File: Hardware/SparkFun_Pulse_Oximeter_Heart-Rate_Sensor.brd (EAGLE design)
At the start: 5 parts, among them U1 MAX30101EFD+T, U2 MAX32664GWEA+T, U3 1.8V/100mA

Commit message: Adds a few parts (end of day merge)
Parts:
- added U$2: PAM2401, SparkFun-IC-Power:MSOP8
- moved U3 10.5 mm to (7.87, 17.8), turned to 0 degrees
- moved U2 7.89 mm to (12.7, 18.0)
- moved U1 3.54 mm to (12.7, 12.7)
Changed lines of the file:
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@@
 </element>
 <element name="U$1" library="SparkX" package="QWIIC_BOARD_MOUNT_NOHOLES" value="QWIIC_BOARD_OUTLINENH" x="12.7" y="12.7" smashed="yes"/>
-<element name="U1" library="temp" package="14_PIN_OESIP" value="MAX30101EFD+T" x="11.43" y="16.002" smashed="yes">
-<attribute name="NAME" x="10.43" y="22.002" size="1" layer="25"/>
-<attribute name="PROD_ID" value="IC-14270" x="11.43" y="16.002" size="1.778" layer="27" font="vector" ratio="15" display="off"/>
-<attribute name="VALUE" x="10.43" y="14.605" size="1" layer="27"/>
+<element name="U3" library="SparkFun-IC-Power" package="SC70" value="1.8V/100mA" x="7.874" y="17.78" smashed="yes">
+<attribute name="NAME" x="6.604" y="17.78" size="0.6096" layer="25" font="vector" ratio="20" rot="R90" align="bottom-center"/>
+<attribute name="PROD_ID" value="VREG-08428" x="7.874" y="17.78" size="1.778" layer="27" font="vector" ratio="15" display="off"/>
+<attribute name="VALUE" x="9.144" y="17.78" size="0.6096" layer="27" font="vector" ratio="20" rot="R90" align="top-center"/>
 </element>
-<element name="U2" library="temp" package="16_PIN_WLP" value="MAX32664GWEA+T" x="10.668" y="10.414" smashed="yes">
-<attribute name="NAME" x="10.668" y="12.414" size="1" layer="25"/>
-<attribute name="PROD_ID" value="IC-14271" x="10.668" y="10.414" size="1.778" layer="27" font="vector" ratio="15" display="off"/>
-<attribute name="VALUE" x="10.668" y="8.914" size="1" layer="27"/>
+<element name="U$2" library="SparkFun-IC-Power" package="MSOP8" value="PAM2401" x="12.446" y="6.604" smashed="yes" rot="R90">
+<attribute name="NAME" x="13.716" y="4.064" size="0.4064" layer="25" rot="R180"/>
+<attribute name="PROD_ID" value="IC-13769" x="12.446" y="6.604" size="1.778" layer="27" rot="R90" display="off"/>
+<attribute name="VALUE" x="13.716" y="9.144" size="0.4064" layer="27" rot="R180"/>
 </element>
-<element name="U3" library="SparkFun-IC-Power" package="SC70" value="1.8V/100mA" x="18.034" y="20.32" smashed="yes" rot="R90">
-<attribute name="NAME" x="18.034" y="19.05" size="0.6096" layer="25" font="vector" ratio="20" rot="R180" align="bottom-center"/>
-<attribute name="PROD_ID" value="VREG-08428" x="18.034" y="20.32" size="1.778" layer="27" font="vector" ratio="15" rot="R90" display="off"/>
-<attribute name="VALUE" x="18.034" y="21.59" size="0.6096" layer="27" font="vector" ratio="20" rot="R180" align="top-center"/>
+<element name="U1" library="temp" package="14_PIN_OESIP" value="MAX30101EFD+T" x="12.7" y="12.7" smashed="yes">
+<attribute name="NAME" x="10.062459375" y="15.909809375" size="1" layer="25"/>
+<attribute name="PROD_ID" value="IC-14270" x="12.7" y="12.7" size="1.778" layer="27" display="off"/>
+<attribute name="VALUE" x="10.062459375" y="8.512809375" size="1" layer="27"/>
+</element>
+<element name="U2" library="temp" package="16_PIN_WLP" value="MAX32664GWEA+T" x="12.7" y="18.034" smashed="yes">
+<attribute name="NAME" x="11.908" y="19.252" size="1" layer="25"/>
+<attribute name="PROD_ID" value="IC-14271" x="12.7" y="18.034" size="1.778" layer="27" display="off"/>
+<attribute name="VALUE" x="11.908" y="15.752" size="1" layer="27"/>
 </element>
 </elements>
@@
 <contactref element="U1" pad="P11"/>
 <contactref element="U2" pad="P$3"/>
-<wire x1="14.275" y1="18.801" x2="11.628" y2="11.714" width="0" layer="19" extent="1-1"/>
+<wire x1="13.907459375" y1="12.708809375" x2="12.868" y2="18.552" width="0" layer="19" extent="1-1"/>
 </signal>
 <signal name="GND">
@@
 <contactref element="U1" pad="P12"/>
 <contactref element="U2" pad="P$13"/>
-<wire x1="11.875" y1="18.801" x2="11.278" y2="11.364" width="0" layer="19" extent="1-1"/>
-<wire x1="14.275" y1="19.601" x2="11.875" y2="18.801" width="0" layer="19" extent="1-1"/>
+<wire x1="11.507459375" y1="12.708809375" x2="12.518" y2="18.202" width="0" layer="19" extent="1-1"/>
+<wire x1="13.907459375" y1="13.508809375" x2="11.507459375" y2="12.708809375" width="0" layer="19" extent="1-1"/>
 </signal>
 <signal name="VDD_LED">
 <contactref element="U1" pad="P10"/>
 <contactref element="U1" pad="P9"/>
-<wire x1="14.275" y1="17.201" x2="14.275" y2="18.001" width="0" layer="19" extent="1-1"/>
+<wire x1="13.907459375" y1="11.108809375" x2="13.907459375" y2="11.908809375" width="0" layer="19" extent="1-1"/>
 </signal>
 <signal name="VCORE">

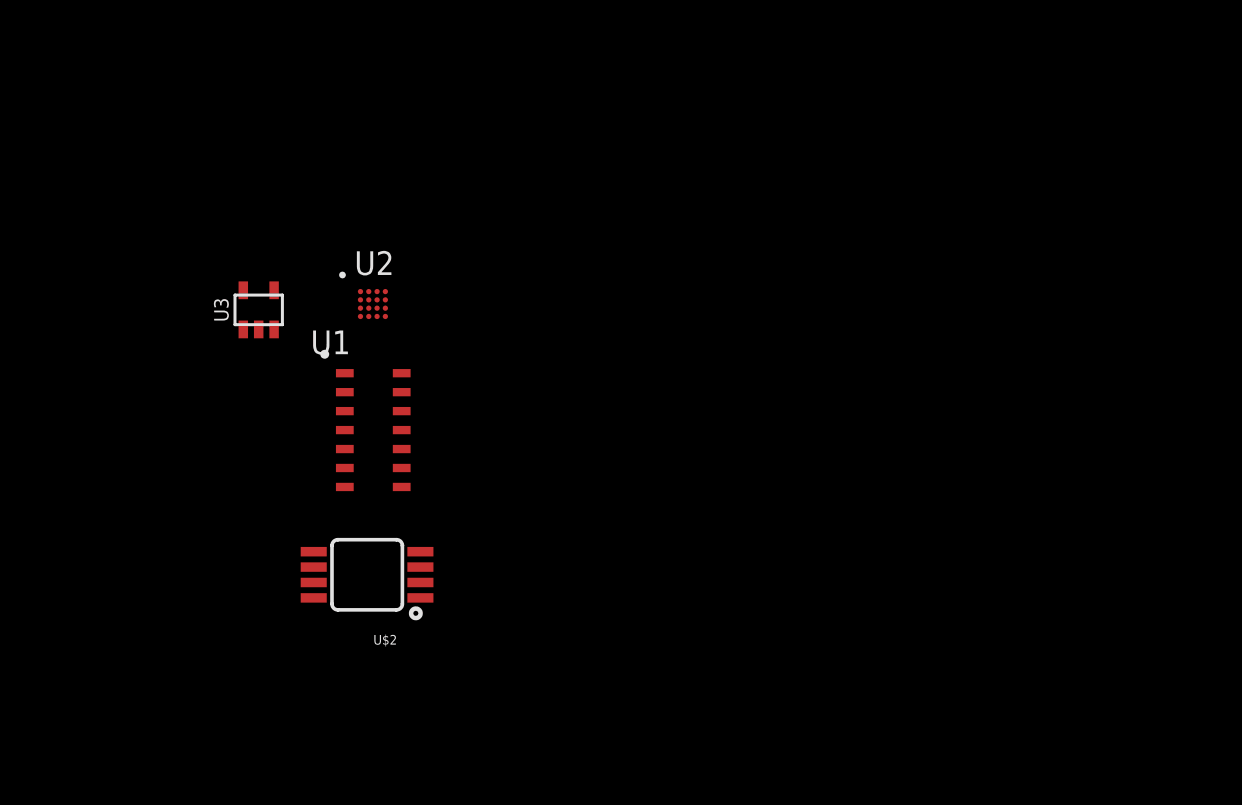
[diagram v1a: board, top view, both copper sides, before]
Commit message: Adds parts to DC-DC converter
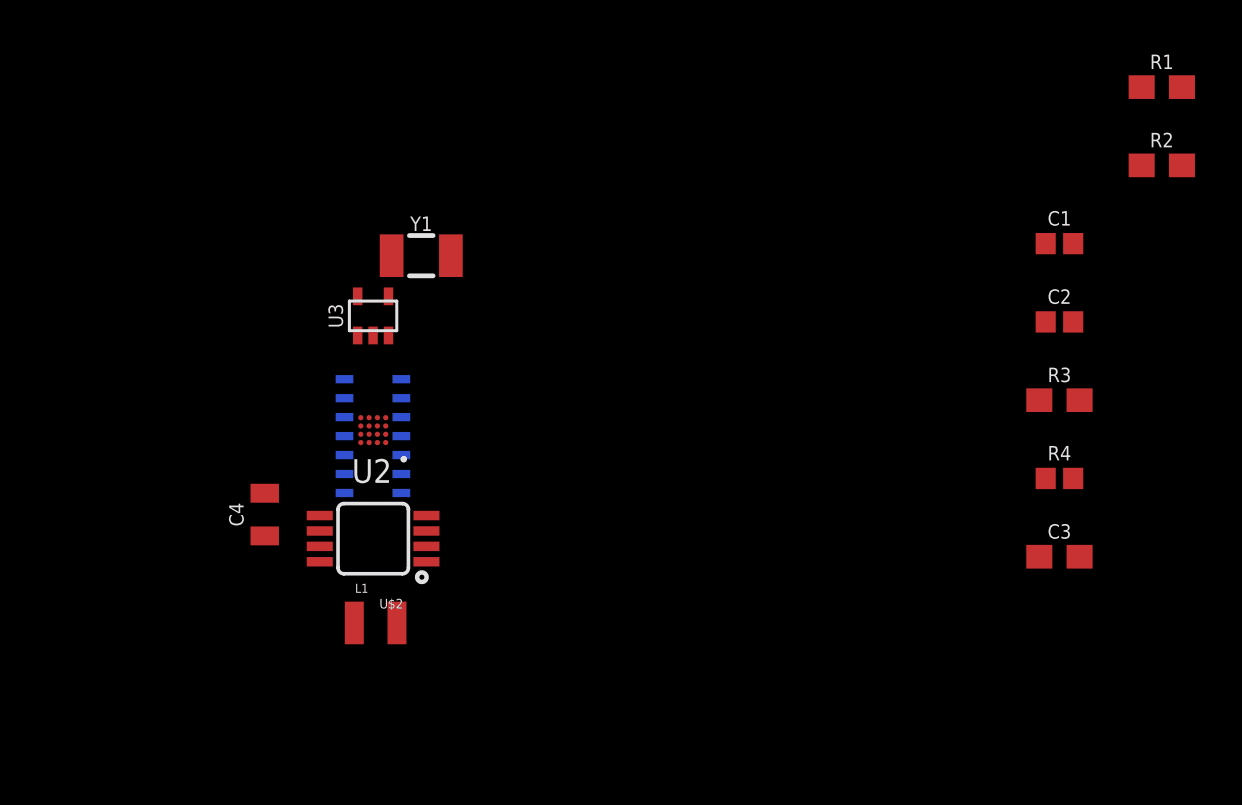
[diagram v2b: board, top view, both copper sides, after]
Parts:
- added C1, C2: 0.1uF, SparkFun-Capacitors:0402
- added C3: 10uF, SparkFun-Capacitors:0603
- added C4: 22uF, SparkFun-Capacitors:0805
- added L1: 2.2μH, SparkFun-Coils:0806
- added R1, R2: 4.7k, SparkFun-Resistors:0603
- added R3: 750K, SparkFun-Resistors:0603
- added R4: 100K, SparkFun-Resistors:0402
- added Y1: 32.768kHz, SparkFun-Clocks:CRYSTAL-SMD-3.2X1.5MM
- moved U2 5.33 mm to (12.7, 12.7), turned to 180 degrees
- moved U3 4.83 mm to (12.7, 17.5)
- moved U$2 1.55 mm to (12.7, 8.13)
- moved U1 0.25 mm to (12.7, 12.4), flipped to the bottom
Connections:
- new net 1.8V: U3.5
- new net 3.3V: C3.1, L1.1, U$2.2, U$2.3, U3.1, U3.3
- new net 5V: C4.1, R3.2, U$2.7
- new net N$2: R3.1, R4.2, U$2.5
- new net N$3: L1.2, U$2.1
- net GND: now also C3.2, C4.2, R4.1, U$2.4, U$2.8, U3.2

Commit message: Many traces and parts have been added, too many to list.
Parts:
- removed U$1: QWIIC_BOARD_OUTLINENH, SparkX:QWIIC_BOARD_MOUNT_NOHOLES
- added C5: 1.0uF, SparkFun-Capacitors:0603
- added C6, C7: 1.0uF, SparkFun-Capacitors:0402
- added J1: (no value), SparkFun-Connectors:JST04_1MM_RA
- added J3: (no value), SparkFun-Connectors:1X04_NO_SILK
- added JP1: JUMPER-SMT_3_2-NC_TRACE_SILK, SparkFun-Jumpers:SMT-JUMPER_3_2-NC_TRACE_SILK
- added R5, R6, R7: 4.7k, SparkFun-Resistors:0603
- C1: value 0.1uF -> 10uF; device SparkFun-Capacitors:0402 -> SparkFun-Capacitors:0603
- moved R1 39.5 mm to (10.7, 9.40), flipped to the bottom
- moved R2 37.6 mm to (10.7, 10.9), flipped to the bottom
- moved FRAME1 35.9 mm to (-4.32, -10.2)
- moved C2 34.0 mm to (10.4, 3.81), flipped to the bottom
- moved C1 32.8 mm to (13.5, 3.81), flipped to the bottom, turned to 180 degrees
- moved R3 25.7 mm to (18.0, 3.81), turned to 270 degrees
- moved R4 24.0 mm to (18.0, 6.60), turned to 270 degrees
- moved C3 21.6 mm to (20.3, 10.4), turned to 180 degrees
- moved Y1 18.0 mm to (3.56, 5.99), turned to 90 degrees
- moved C4 14.7 mm to (21.1, 2.29), turned to 0 degrees
- moved L1 11.8 mm to (23.6, 10.2), turned to 270 degrees
- moved U3 10.6 mm to (7.37, 8.38), flipped to the bottom
- moved U2 8.80 mm to (6.60, 6.35), turned to 90 degrees
- moved U$2 8.57 mm to (21.1, 6.35), turned to 180 degrees
- moved U1 5.86 mm to (12.2, 6.60), turned to 270 degrees
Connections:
- removed net VCORE: U2.P$4
- removed net VDD: U1.P11, U2.P$3
- removed net VDD_LED: U1.P10, U1.P9
- new net !HR_INT: R5.1, U1.P13, U2.P$6
- new net !MFIO: U2.P$16
- new net !RST: U2.P$12
- new net HOST_SCL: J1.4, J3.4, R7.1, U2.P$10
- new net HOST_SDA: J1.3, J3.3, R6.1, U2.P$9
- new net N$1: C7.1, U2.P$4
- new net N$4: JP1.3, R6.2
- new net N$5: JP1.1, R7.2
- new net N$6: U2.P$1, Y1.P$1
- new net N$7: U2.P$2, Y1.P$2
- new net SNSR_SCL: R2.1, U1.P2, U2.P$5
- new net SNSR_SDA: R1.1, U1.P3, U2.P$14
- net 1.8V: now also C2.1, C5.1, C6.1, R1.2, R2.2, R5.2, U1.P11, U2.P$3
- net 3.3V: now also J1.2, J3.2, JP1.2
- net 5V: now also C1.1, U1.P10, U1.P9
- net GND: now also C1.2, C2.2, C5.2, C6.2, C7.2, J1.1, J3.1
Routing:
- net HOST_SDA: track 0.00 -> 17.0 mm, vias 0 -> 1
- net 3.3V: track 0.00 -> 14.9 mm
- net 5V: track 0.00 -> 14.0 mm, vias 0 -> 1
- net 1.8V: track 0.00 -> 11.4 mm
- net HOST_SCL: track 0.00 -> 11.4 mm
- net N$2: track 0.00 -> 3.67 mm
- net SNSR_SCL: track 0.00 -> 3.51 mm
- net N$7: track 0.00 -> 3.20 mm
- net N$6: track 0.00 -> 3.17 mm
- net N$3: track 0.00 -> 1.84 mm
- net SNSR_SDA: track 0.00 -> 1.66 mm
- net N$1: track 0.00 -> 1.55 mm
- added copper zone on layer 1, net GND
- added copper zone on layer 16, net GND
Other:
- board outline added: 25.4 x 12.7 mm
- board text added: "Elias Santistevan"

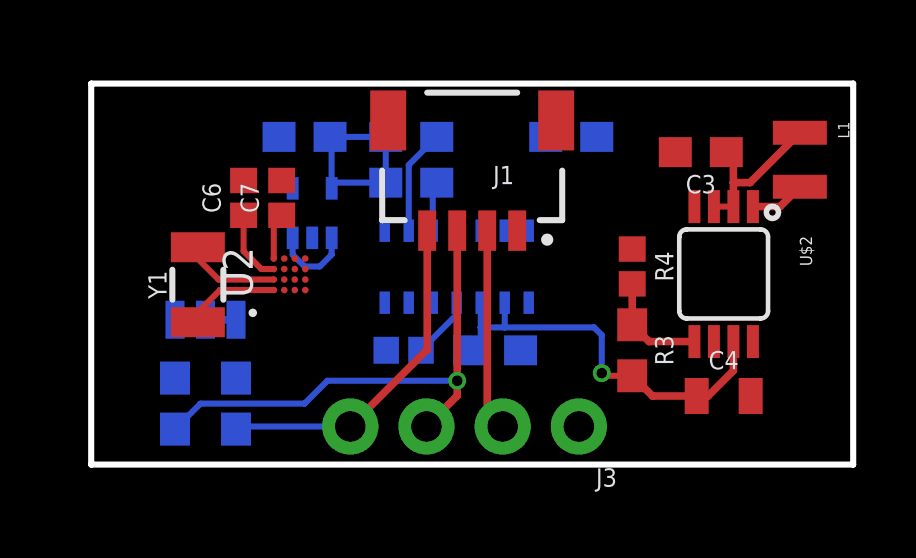
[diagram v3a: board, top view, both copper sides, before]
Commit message: Adds slik, trace work complete, ground vias added throughout design, schematic organized with lables
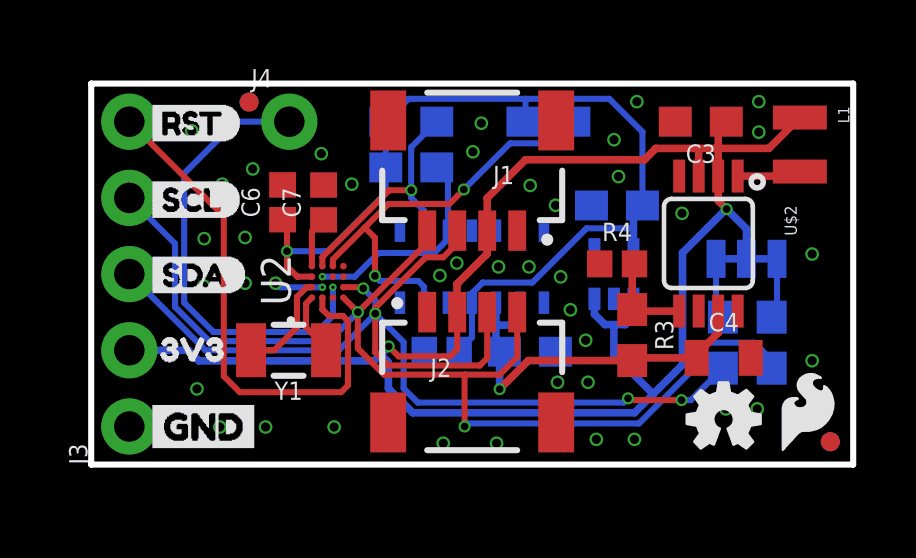
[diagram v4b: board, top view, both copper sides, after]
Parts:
- added FD1, FD2, FD3, FD4: FIDUCIALUFIDUCIAL, SparkFun-Aesthetics:FIDUCIAL-MICRO
- added J2: (no value), SparkFun-Connectors:JST04_1MM_RA
- added J4: (no value), SparkFun-Connectors:1X01_NO_SILK
- added LOGO1: SFE_LOGO_FLAME.1_INCH, SparkFun-Aesthetics:SFE_LOGO_FLAME_.1
- added LOGO2: OSHW-LOGOMINI, SparkFun-Aesthetics:OSHW-LOGO-MINI
- added LOGO3: SFE_LOGO_NAME.1_INCH, SparkFun-Aesthetics:SFE_LOGO_NAME_.1
- added U$1: (no value), Labels:I_SUPER2_C-()-03
- added U$10, U$4: (no value), buzzard_labels:SCL0
- added U$11, U$3: (no value), Labels:GND-03
- added U$12: (no value), Labels:3V3-03
- added U$13: (no value), Labels:3V3-TEXT
- added U$14: (no value), oximeter:OXIMETER0
- added U$15: (no value), Heart Rate:HEART_RATE0
- added U$16: (no value), Monitor:MONITOR0
- added U$5, U$9: (no value), SDA:SDA0
- added U$6, U$8: (no value), RST:RST0
- added U$7: (no value), MFIO:MFIO0
- J3: device SparkFun-Connectors:1X04_NO_SILK -> SparkFun-Connectors:1X05_NO_SILK
- moved R6 18.4 mm to (21.1, 4.06)
- moved JP1 18.1 mm to (21.8, 6.86)
- moved R7 18.0 mm to (22.7, 4.06)
- moved J3 15.0 mm to (1.27, 1.27), turned to 90 degrees
- moved C5 10.7 mm to (17.5, 8.64)
- moved U3 10.3 mm to (17.4, 6.35)
- moved Y1 3.73 mm to (6.58, 3.81), turned to 180 degrees
- moved C7 1.41 mm to (7.75, 8.74)
- moved C6 1.31 mm to (6.38, 8.74)
- moved U2 1.30 mm to (7.87, 6.10)
- moved C4 1.27 mm to (21.1, 3.56)
- moved C2 1.27 mm to (11.7, 3.81)
- moved C1 1.16 mm to (14.6, 3.76)
- moved U$2 1.14 mm to (20.6, 7.37)
- moved C3 1.02 mm to (20.3, 11.4)
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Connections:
- net !HR_INT: now also U2.6; no longer U2.P$6
- net !MFIO: now also J4.1, U2.16; no longer U2.P$16
- net !RST: now also J3.5, U2.12; no longer U2.P$12
- net 1.8V: now also U2.3; no longer U2.P$3
- net 3.3V: now also J2.2
- net GND: now also J2.1, U2.13; no longer U2.P$13
- net HOST_SCL: now also J2.4, U2.10; no longer U2.P$10
- net HOST_SDA: now also J2.3, U2.9; no longer U2.P$9
- net N$1: now also U2.4; no longer U2.P$4
- net N$6: now also U2.1; no longer U2.P$1
- net N$7: now also U2.2; no longer U2.P$2
- net SNSR_SCL: now also U2.5; no longer U2.P$5
- net SNSR_SDA: now also U2.14; no longer U2.P$14
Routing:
- net 3.3V: track 14.9 -> 57.9 mm, vias 0 -> 2
- net HOST_SCL: track 11.4 -> 38.1 mm, vias 0 -> 2
- net 1.8V: track 11.4 -> 31.6 mm, vias 0 -> 1
- net HOST_SDA: track 17.0 -> 36.8 mm, vias 1 -> 4
- net !RST: track 0.00 -> 17.8 mm
- net !MFIO: track 0.00 -> 15.1 mm, vias 0 -> 1
- net !HR_INT: track 0.00 -> 14.2 mm, vias 0 -> 2
- net SNSR_SDA: track 1.66 -> 7.26 mm, vias 0 -> 1
- net SNSR_SCL: track 3.51 -> 8.35 mm, vias 0 -> 1
- net N$4: track 0.00 -> 2.04 mm
- net N$5: track 0.00 -> 2.02 mm
- net GND: track 0.00 -> 1.62 mm, vias 0 -> 42
- net N$6: track 3.17 -> 2.11 mm
- net N$2: track 3.67 -> 3.14 mm
- net 5V: track 14.0 -> 13.5 mm
